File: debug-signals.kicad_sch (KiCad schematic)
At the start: 77 parts

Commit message: Cosmetic changes
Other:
- moved on the sheet: C?, R?, U?

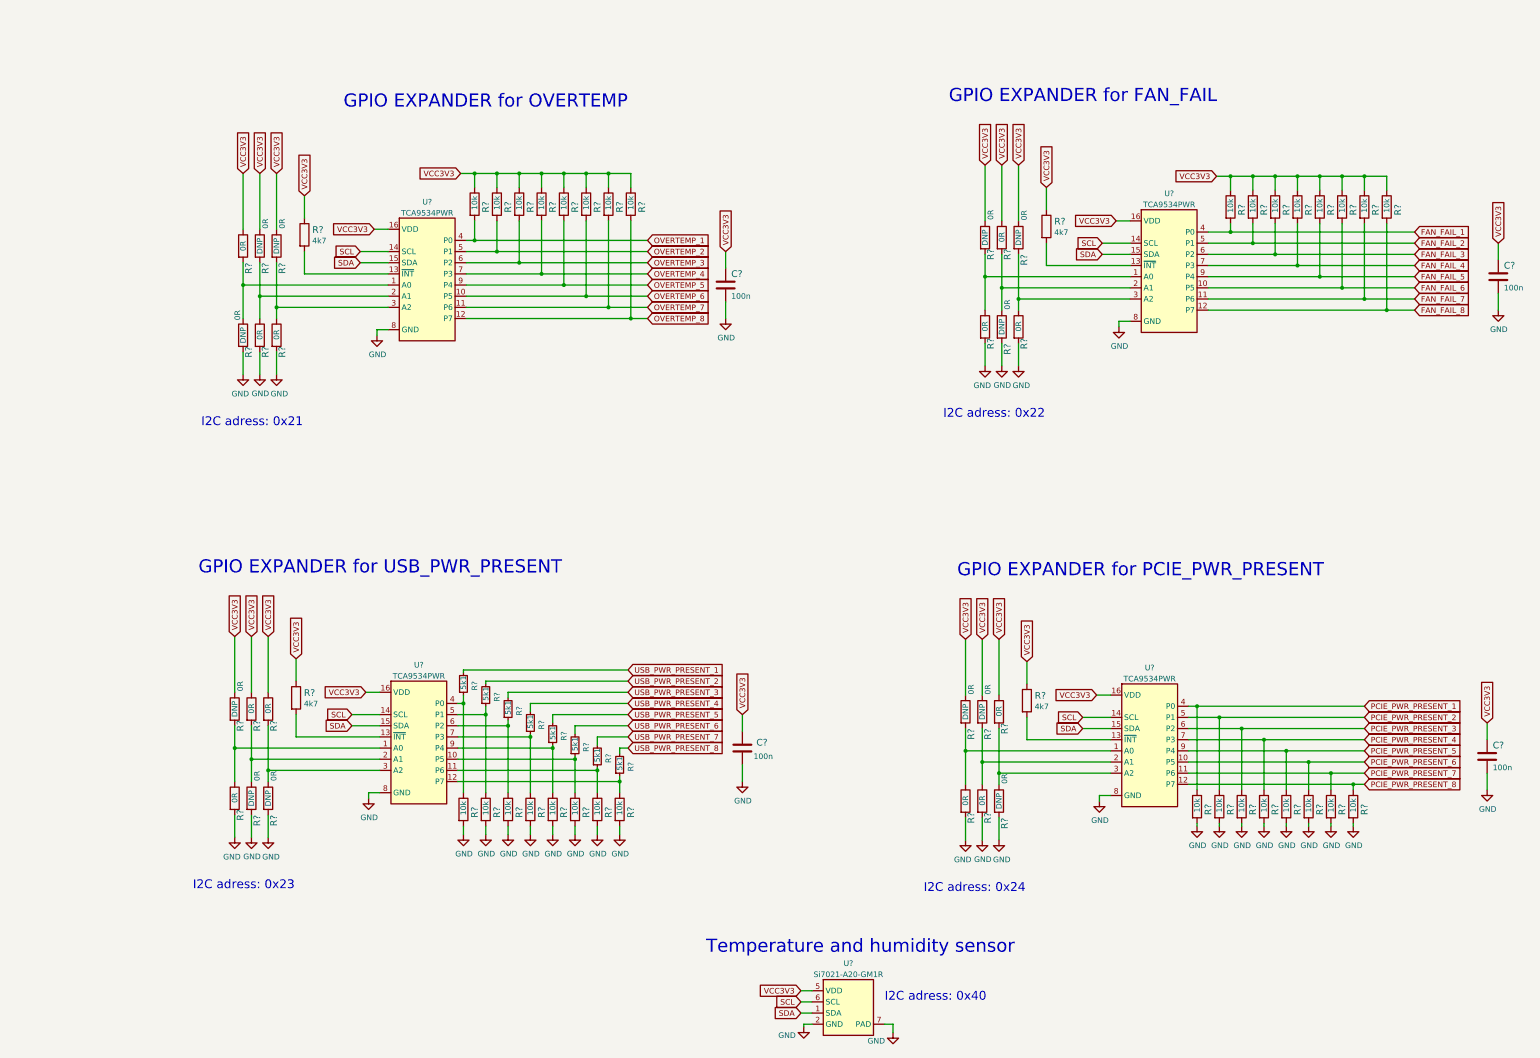
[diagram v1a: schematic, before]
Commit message: Rearange hierarchical schematics
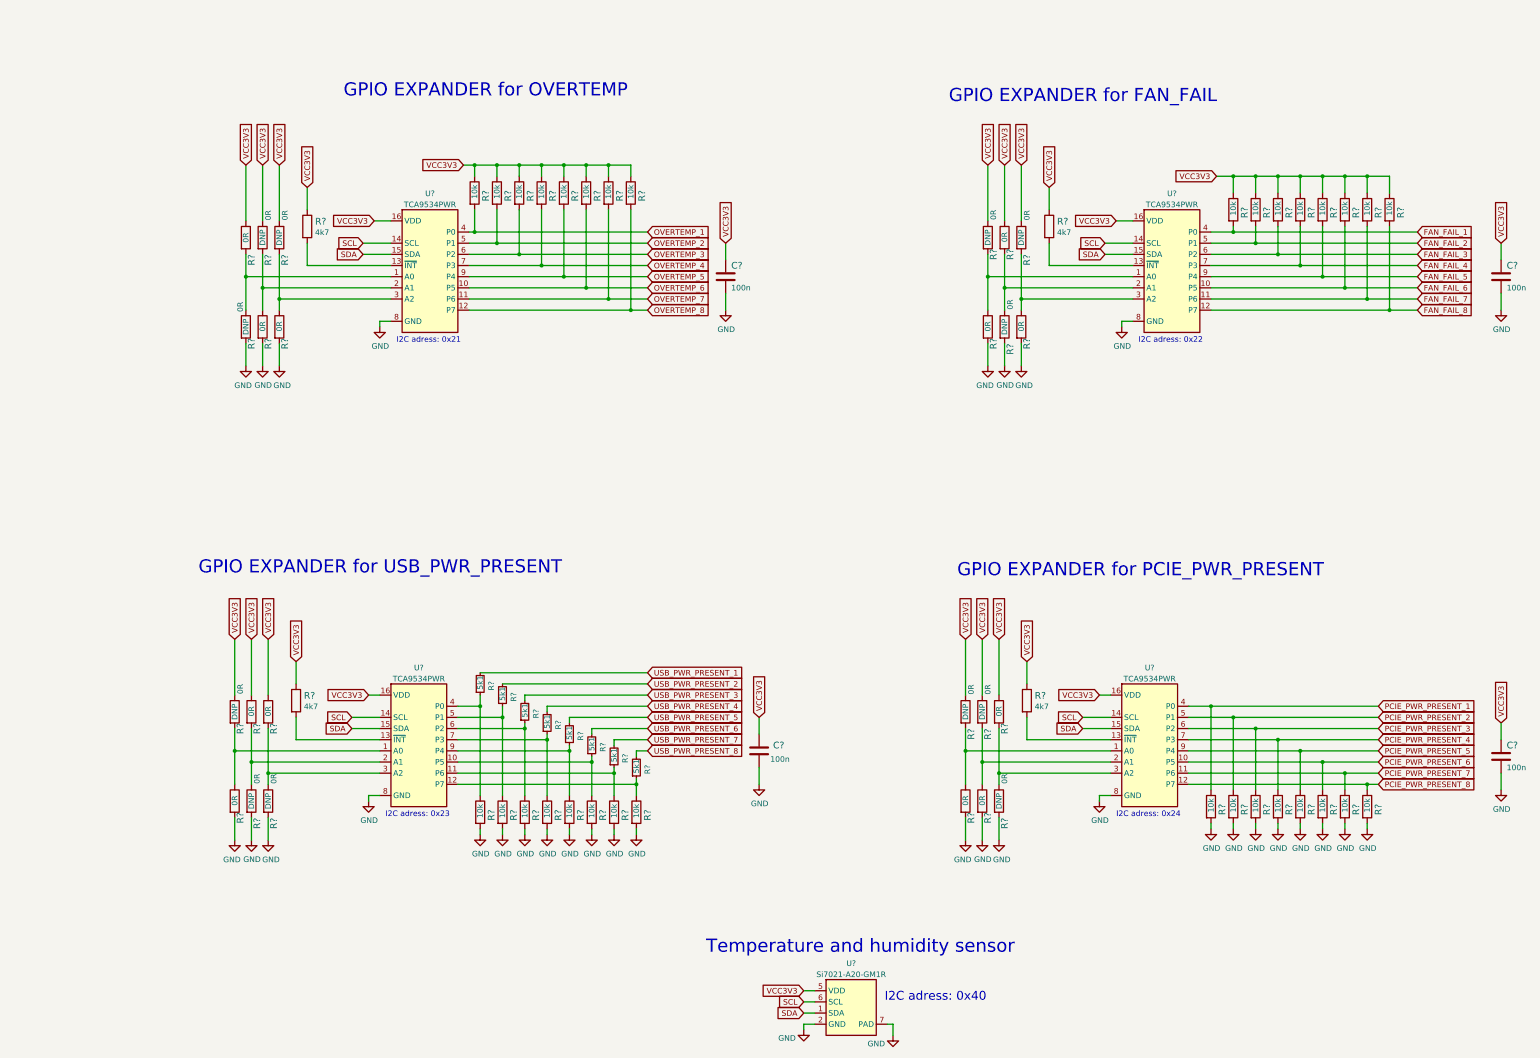
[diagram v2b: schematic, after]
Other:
- moved on the sheet: C?, R?, U?

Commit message: Change power flags on schematic
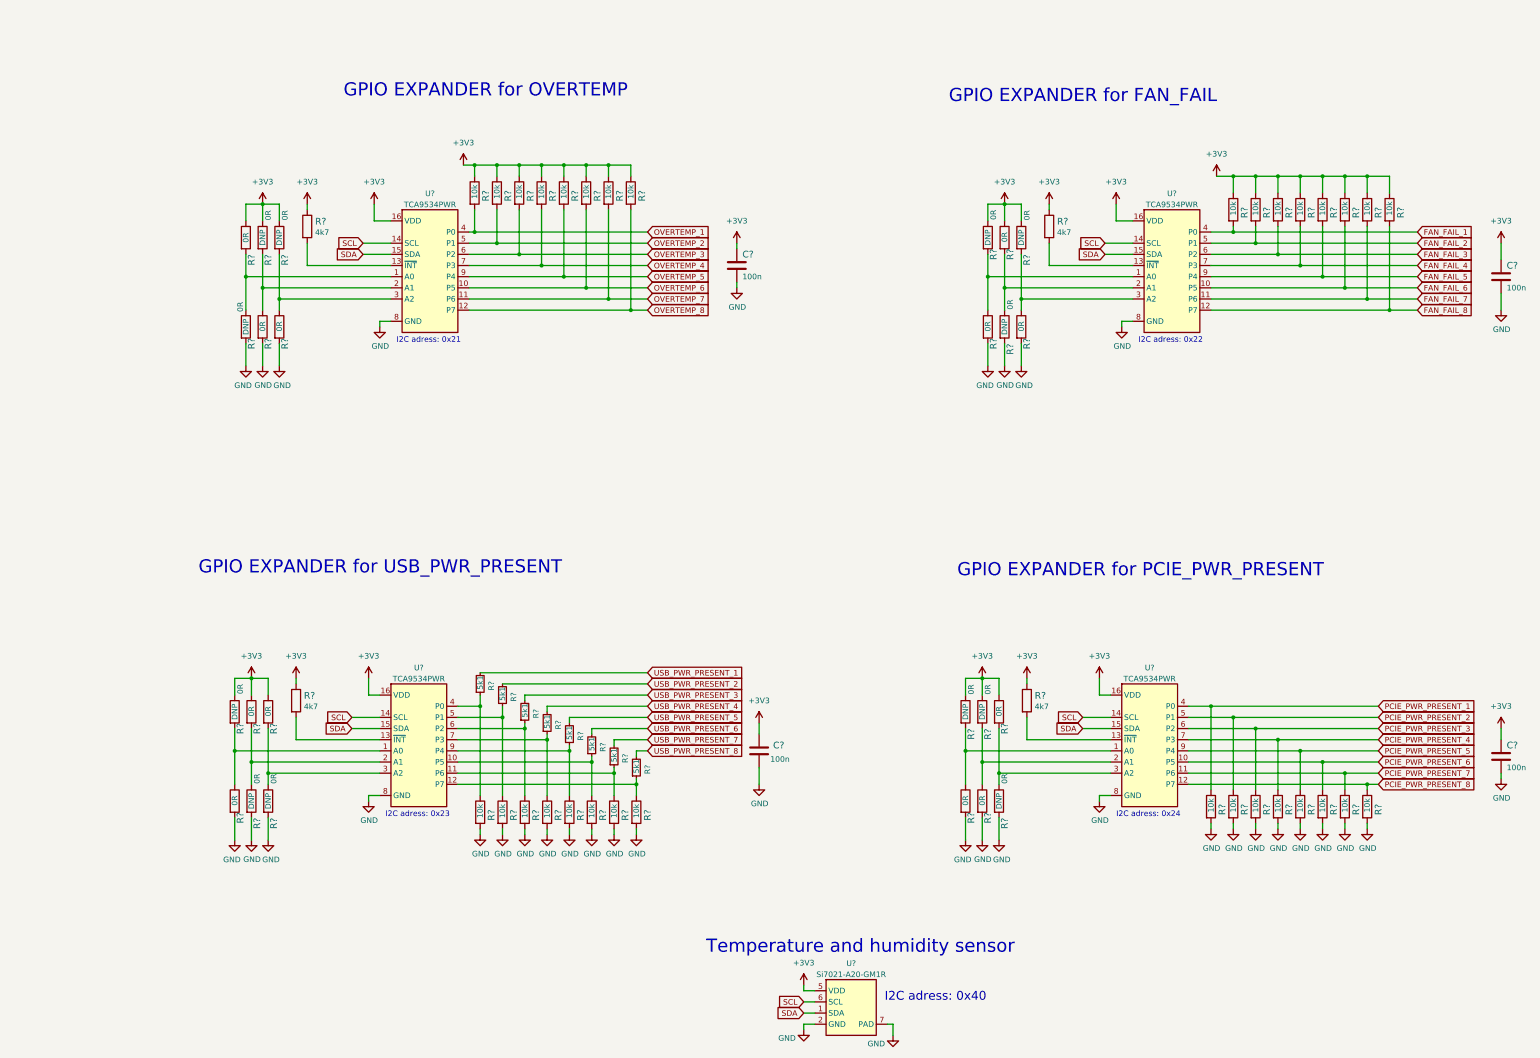
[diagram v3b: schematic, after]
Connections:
- net VCC3V3 renamed +3V3
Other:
- moved on the sheet: C?

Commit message: Reannotate schematic symbols
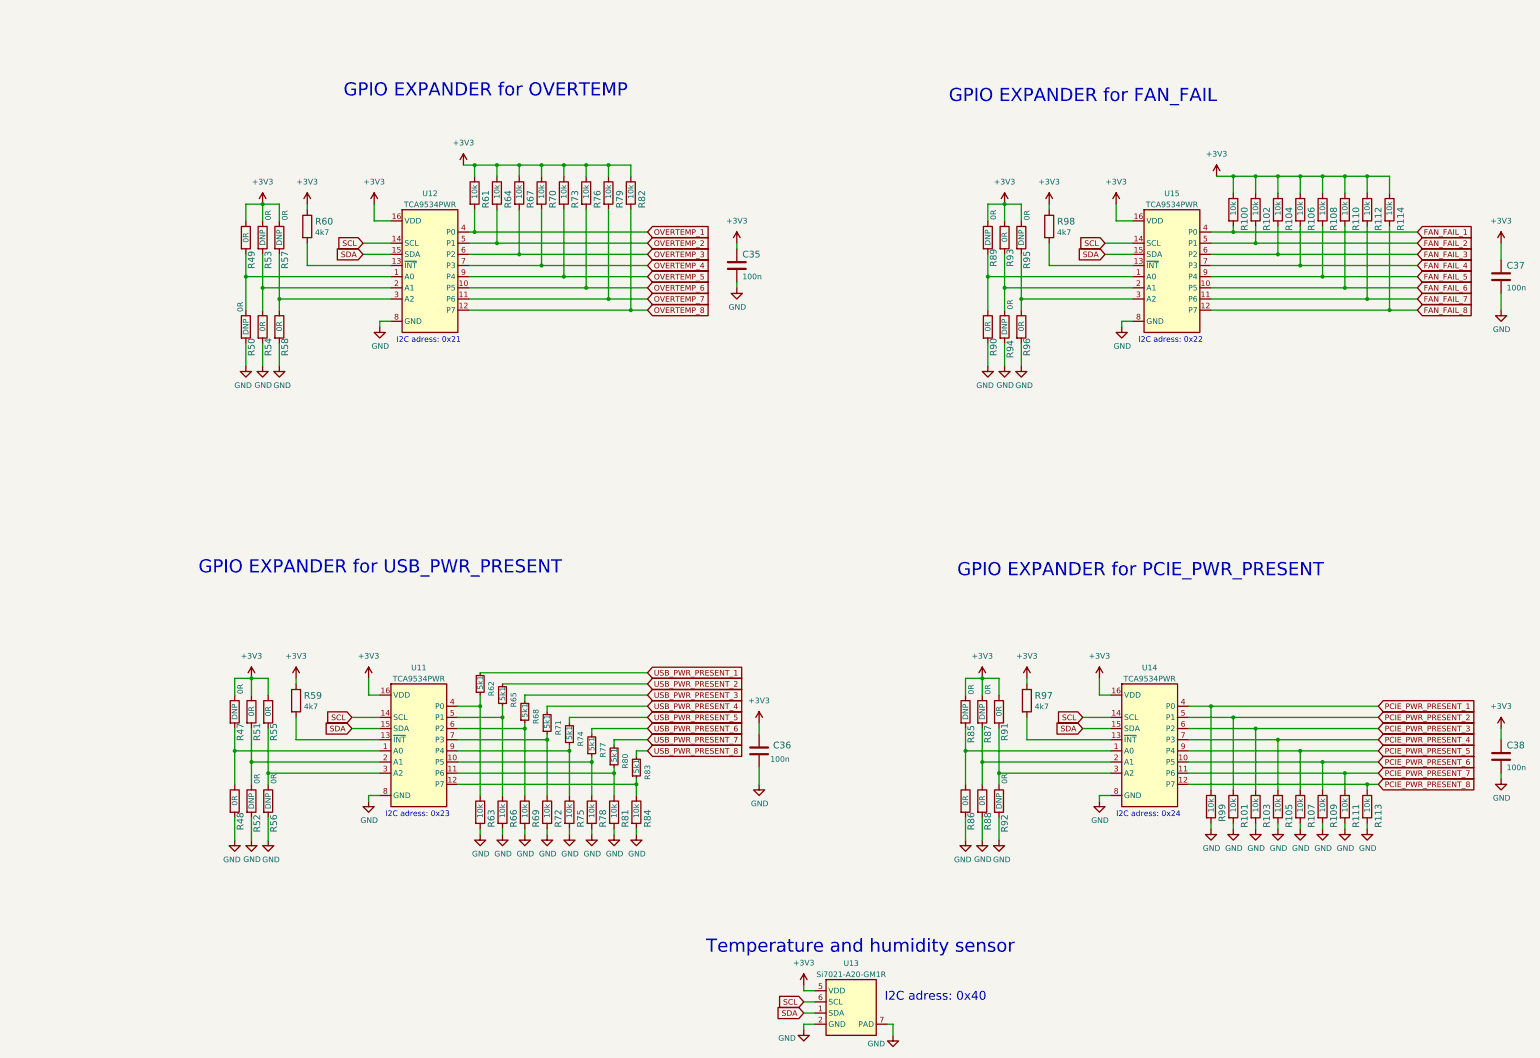
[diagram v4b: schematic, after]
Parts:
- gave numbers to parts that had none: 77

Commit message: Set resitsors to standard
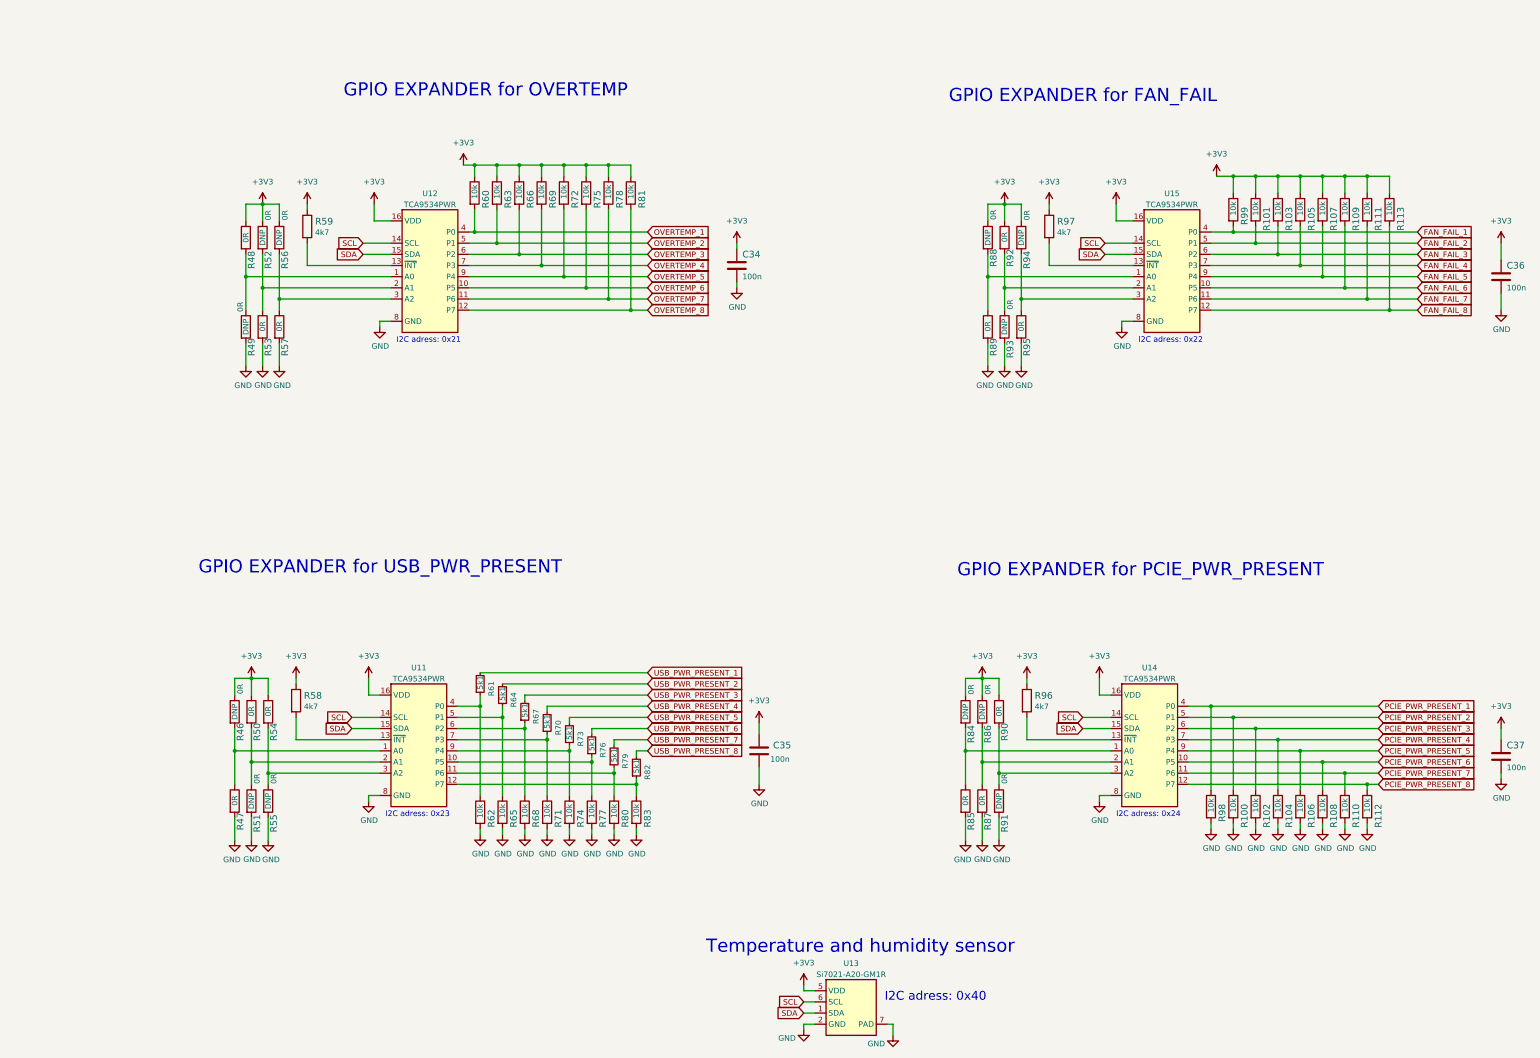
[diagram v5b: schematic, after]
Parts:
- renumbered C35 to C34, C36 to C35, C37 to C36, C38 to C37, R101 to R100, R102 to R101, R103 to R102, R104 to R103, R105 to R104, R106 to R105, R107 to R106, R108 to R107, R109 to R108, R110 to R109, R111 to R110, R112 to R111, R113 to R112, R114 to R113, R47 to R46, R48 to R47, R49 to R48, R50 to R49, R51 to R50, R52 to R51, R53 to R52, R54 to R53, R55 to R54, R56 to R55, R57 to R56, R58 to R57, R59 to R58, R60 to R59, R61 to R60, R62 to R61, R63 to R62, R64 to R63, R65 to R64, R66 to R65, R67 to R66, R68 to R67, R69 to R68, R70 to R69, R71 to R70, R72 to R71, R73 to R72, R74 to R73, R75 to R74, R76 to R75, R77 to R76, R78 to R77, R79 to R78, R80 to R79, R81 to R80, R82 to R81, R83 to R82, R84 to R83, R85 to R84, R86 to R85, R87 to R86, R88 to R87, R89 to R88, R90 to R89, R91 to R90, R92 to R91, R93 to R92, R94 to R93, R95 to R94, R96 to R95, R97 to R96, R98 to R97, R99 to R98, R100 to R99

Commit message: Repleace non standard components in connectors and ftdi and power
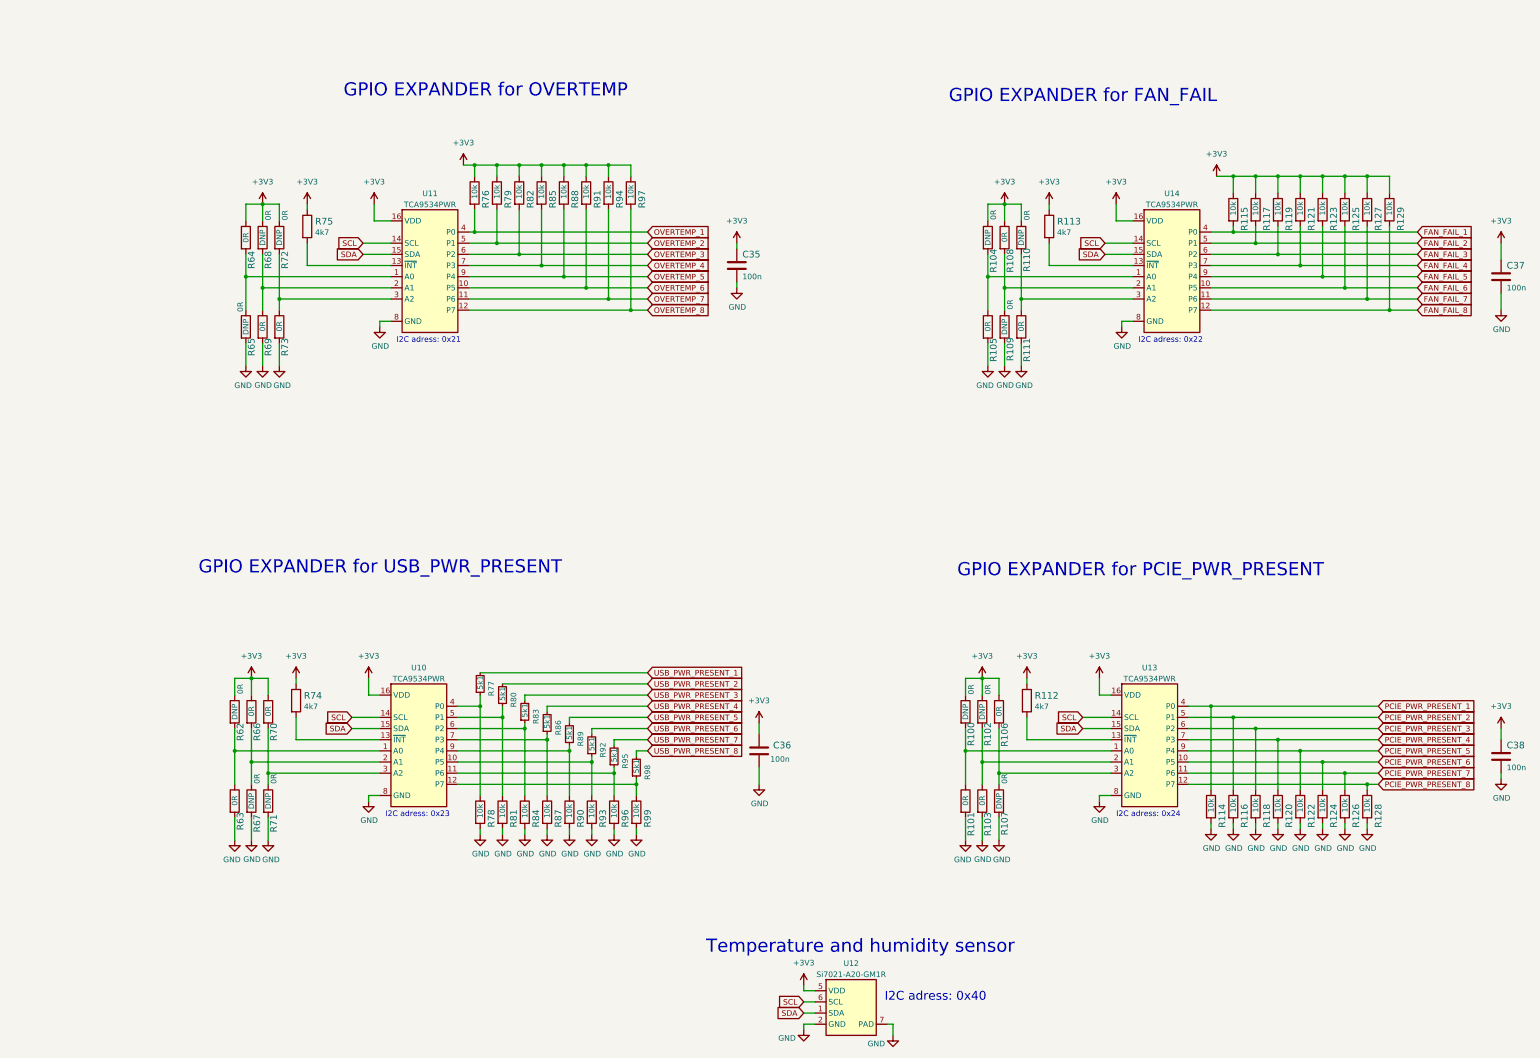
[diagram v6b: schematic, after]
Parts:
- renumbered C34 to C35, C35 to C36, C36 to C37, C37 to C38, R84 to R100, R85 to R101, R86 to R102, R87 to R103, R88 to R104, R89 to R105, R90 to R106, R91 to R107, R92 to R108, R93 to R109, R94 to R110, R95 to R111, R96 to R112, R97 to R113, R98 to R114, R99 to R115, R100 to R116, R101 to R117, R102 to R118, R103 to R119, R104 to R120, R105 to R121, R106 to R122, R107 to R123, R108 to R124, R109 to R125, R110 to R126, R111 to R127, R112 to R128, R113 to R129, R46 to R62, R47 to R63, R48 to R64, R49 to R65, R50 to R66, R51 to R67, R52 to R68, R53 to R69, R54 to R70, R55 to R71, R56 to R72, R57 to R73, R58 to R74, R59 to R75, R60 to R76, R61 to R77, R62 to R78, R63 to R79, R64 to R80, R65 to R81, R66 to R82, R67 to R83, R68 to R84, R69 to R85, R70 to R86, R71 to R87, R72 to R88, R73 to R89, R74 to R90, R75 to R91, R76 to R92, R77 to R93, R78 to R94, R79 to R95, R80 to R96, R81 to R97, R82 to R98, R83 to R99, U11 to U10, U12 to U11, U13 to U12, U14 to U13, U15 to U14
